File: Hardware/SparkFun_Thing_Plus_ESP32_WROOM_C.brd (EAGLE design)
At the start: 22.9 x 58.4 mm, 108 parts, among them J2 MICRO-SDFRICTION, J3 QWIIC_RA, J5 THING_PLUS, Q2 MBT3904DW1T1, Q3 20V/4.2A/52mΩ/1.4W, U1 MCP73831, U2 ESP-WROOM-3232D-NARROW, U3 XC6222B331MR-G, U4 MAX17048, U5 XC6222B331MR-G, U7 CH340C

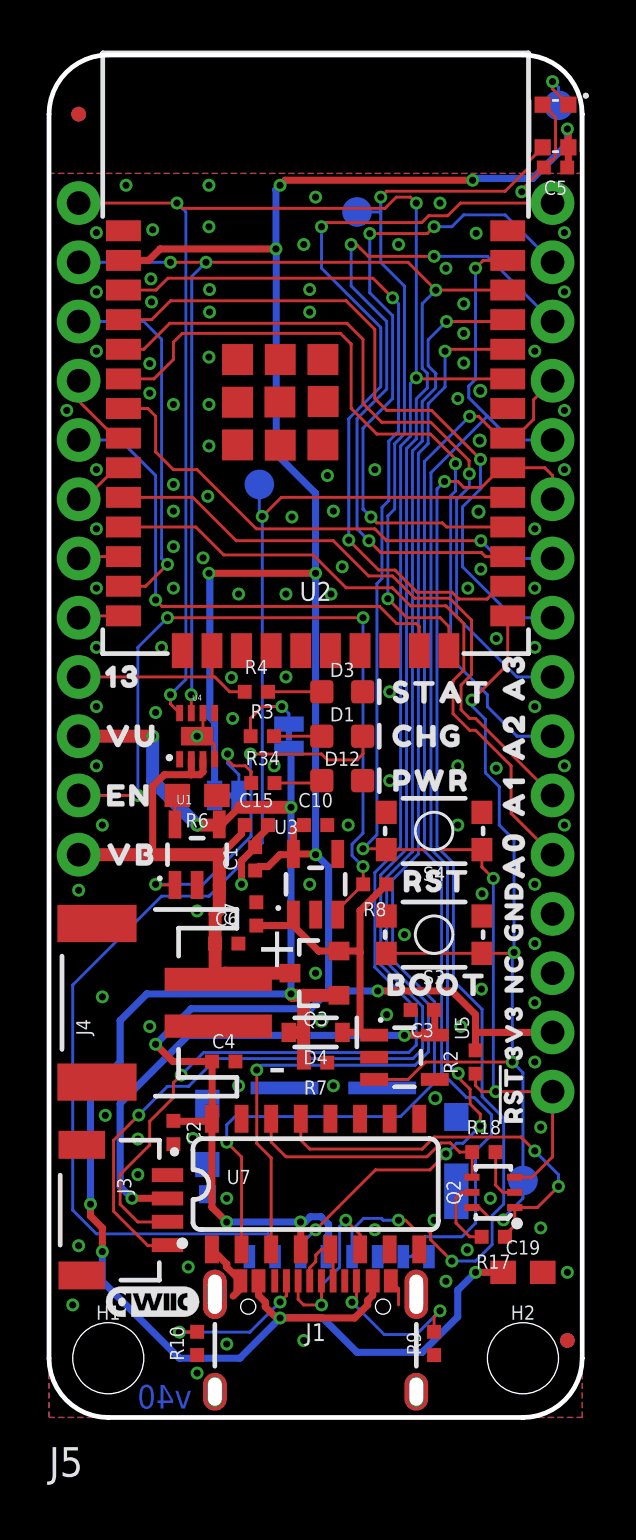
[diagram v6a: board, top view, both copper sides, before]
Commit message: Completed updates post DR.
Schematic:
Change all  text to vector, 8%
Add row lines to boot mode table
Add NC jumper on USB-C shield.
Change 0.1u cap to 10u next to uSD.
Update uSD device to pull in newest changes to keepout.
Label LED jumpers JP1, JP2
Change ADC2 note to say “Is not available when wifi enabled.”
Rearrange schematic to make ESP32 notes fit in box when vectored font.
Change symbol for SOT-25 VREGs to remove NC pin.
Add Nate’s Thing Plus symbol to the SFE libs and make the board change to be logical instead of physical.

Board:
Space out top RGB LED per Dryw’s design
Add dimensions to the uSD card and it’s protrusion.
Add pin 1 indicator for CH340, it’s covered.
Add designed/revised by to board.
Move C19 close to batt charge IC, remove top silk on EN/VB to make it fit if necessary.
Change the width of V_USB to be consistent across the board.
Aim for 30 mil, that’s a 60deg increase at 2A
Got 22 mil all around, best I could do
Change GND, 3.3, NC bottom silk to be pill-style
Fit a flame logo on top.
Acid traps
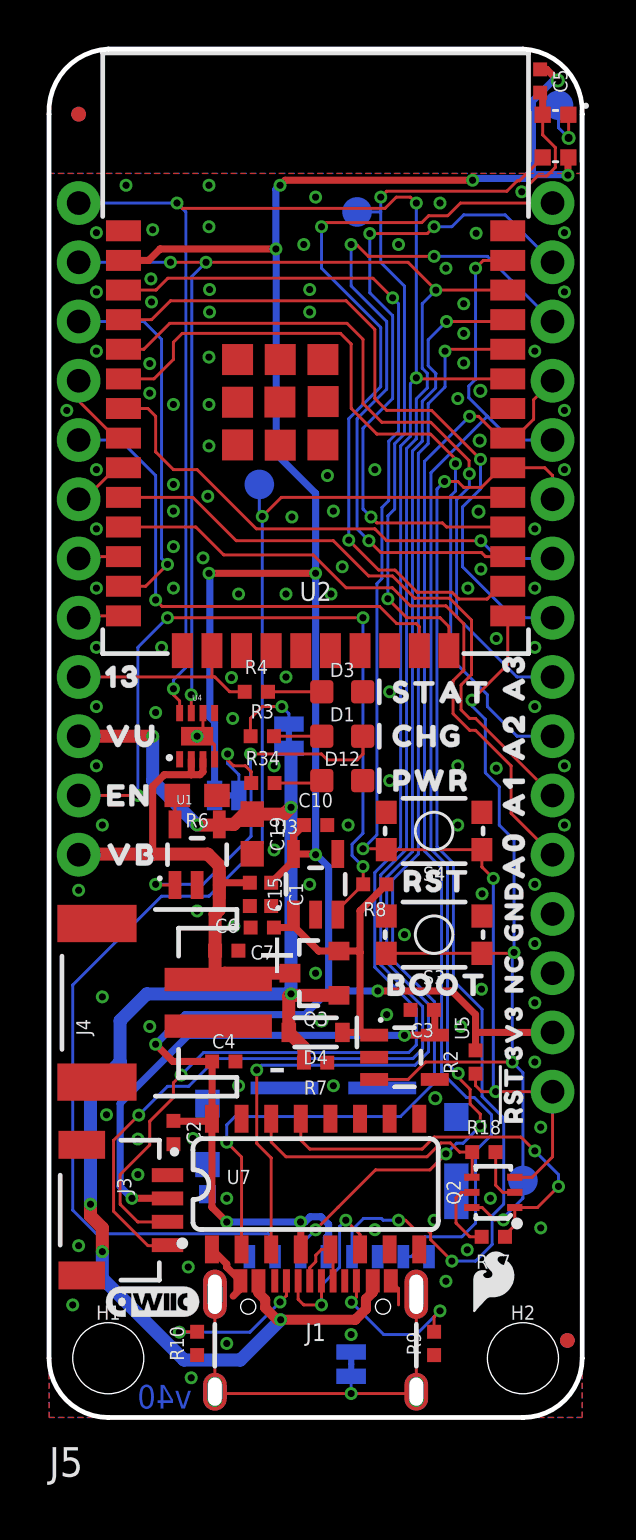
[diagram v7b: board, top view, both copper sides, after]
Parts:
- removed U$106: (no value), output:NC0
- removed U$108: (no value), output:3V30
- removed U$56: (no value), output:GND1
- added JP3: JUMPER-SMT_2_NC_TRACE_SILK, SparkFun-Jumpers:SMT-JUMPER_2_NC_TRACE_SILK
- added U$10: (no value), output:#_NC#0
- added U$11: (no value), output:#_3V3#0
- added U$12: (no value), SparkFun-Aesthetics:SFE_LOGO_FLAME_.1
- added U$8: (no value), output:#SHLD#0
- added U$9: (no value), output:#_GND#0
- C5: value 0.1uF -> 10uF
- J5: value THING_PLUS -> THING_PLUS_LOGICAL
- JP1, JP2: value (none) -> JUMPER-SMT_2_NC_TRACE_SILK
- moved C19 22.1 mm to (8.71, 25.0), turned to 270 degrees
- moved LOGO1 4.38 mm to (7.01, 18.0)
- moved C5 3.77 mm to (21.1, 57.3), turned to 270 degrees
- moved C15 2.98 mm to (8.61, 22.4), turned to 270 degrees
- moved C1 1.67 mm to (9.53, 22.4), turned to 270 degrees
- moved C7 0.64 mm to (9.14, 21.0), turned to 180 degrees
- moved D5 0.43 mm to (21.7, 54.9)
- moved C6 0.30 mm to (7.62, 20.0)
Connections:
- net ESP_12/TP_8 renamed ESP_12/GPIO1
- net ESP_13/TP_9/LED renamed ESP_13/GPIO0/LED
- net ESP_14/TP_3 renamed ESP_14/GPIO6
- net ESP_15/TP_5 renamed ESP_15/GPIO4
- net ESP_27/TP_7 renamed ESP_27/GPIO2
- net ESP_32/TP_4 renamed ESP_32/GPIO5
- net ESP_33/TP_6 renamed ESP_33/GPIO3
- new net N$8: J1.SHLD1, J1.SHLD2, J1.SHLD3, J1.SHLD4, JP3.2
- net GND: now also JP3.1
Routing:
- net N$8: track 0.00 -> 17.8 mm, vias 0 -> 1
- net V_USB: track 77.1 -> 64.9 mm, vias 8 -> 7
- net 3.3V: track 115.9 -> 119.1 mm, vias 11 -> 12
- net GND: track 14.0 -> 11.8 mm
- net VIN: track 13.6 -> 12.9 mm
- net V_BATT: track 23.0 -> 22.3 mm
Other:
- board size 22.9 x 58.4 mm -> 22.9 x 58.7 mm
- board text added: "Alex Brudner"
- board text added: "Nathan Seidle"
- board text added: "Revised by:"

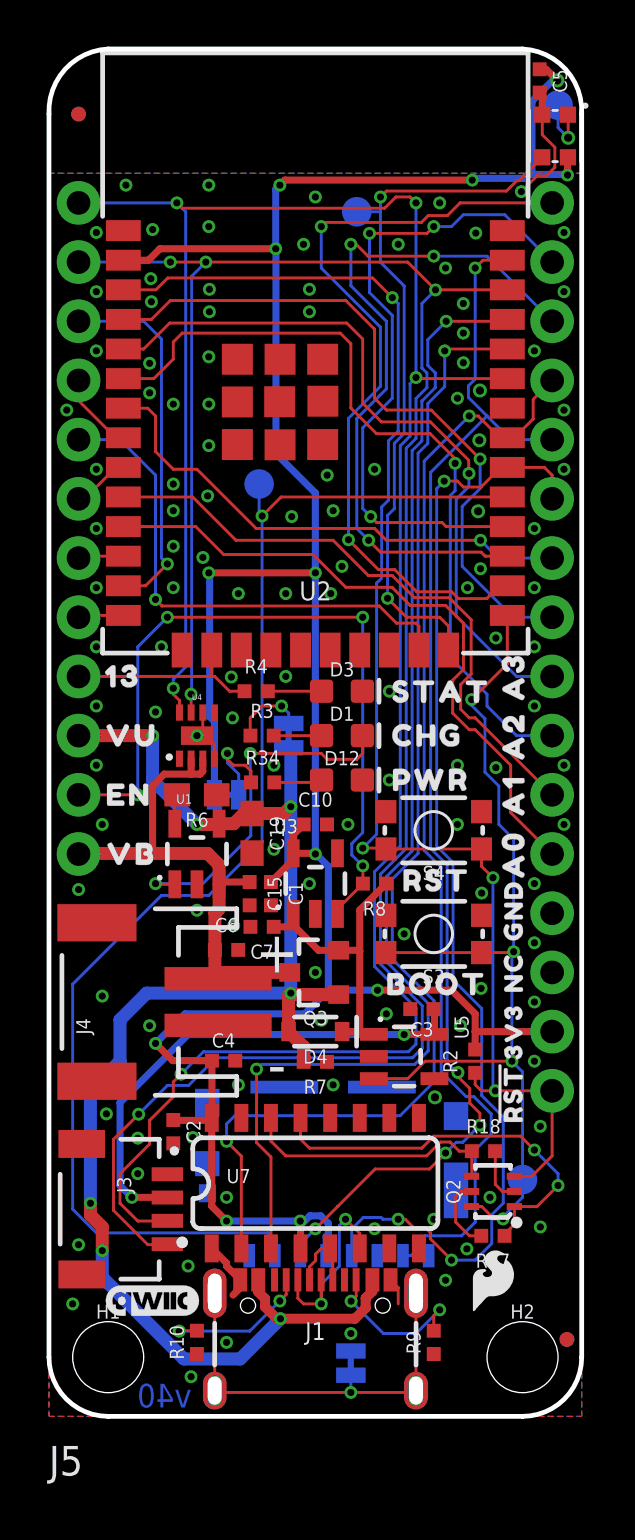
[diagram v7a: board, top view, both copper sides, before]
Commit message: Update post DR changes.
Minor movement edits.
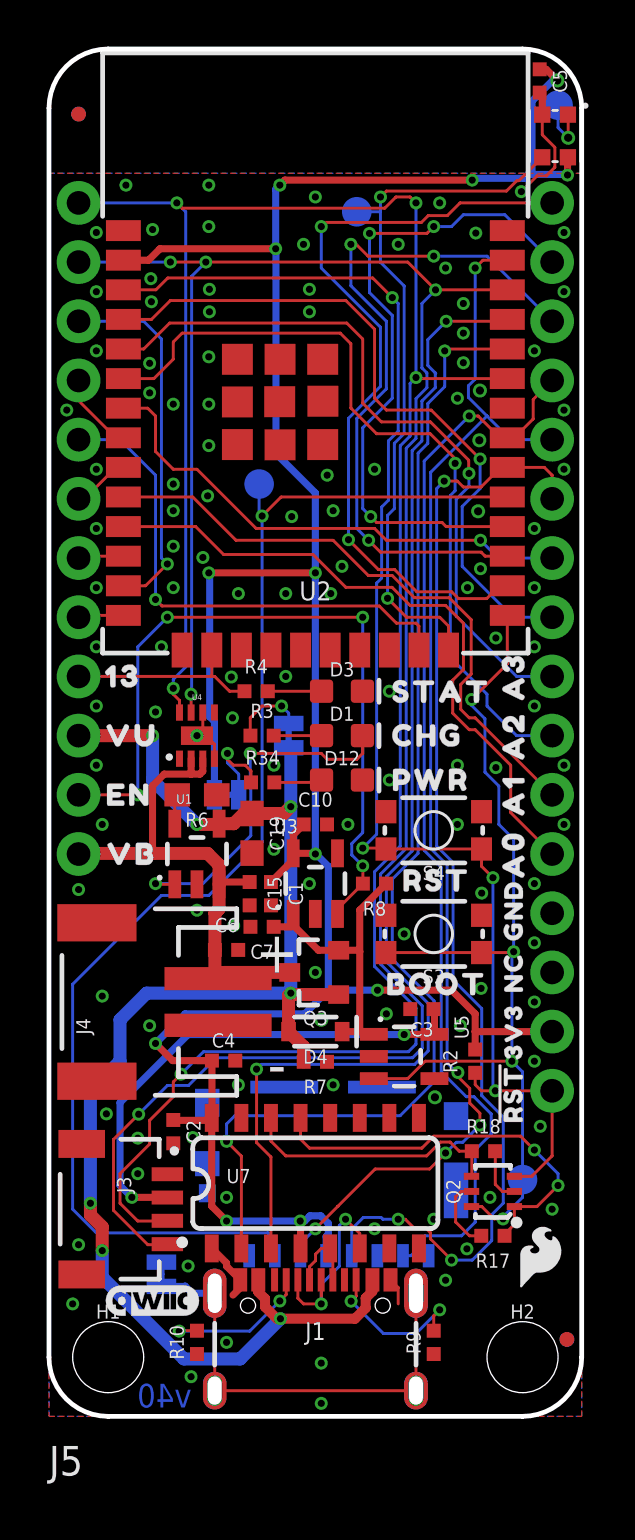
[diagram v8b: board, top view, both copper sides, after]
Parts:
- removed U$59: (no value), SparkFun-Aesthetics:ORDERING_INSTRUCTIONS
- moved LOGO2 19.2 mm to (2.46, 13.0)
- moved U$1 16.8 mm to (21.3, 6.86)
- moved JP3 8.98 mm to (4.83, 6.10)
- moved U$8 8.77 mm to (4.83, 6.93), turned to 90 degrees
- moved U$12 2.27 mm to (21.1, 6.86)
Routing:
- net N$8: track 17.8 -> 19.4 mm, vias 1 -> 0
- net GND: vias 119 -> 120
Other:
- outline, holes or cut-outs redrawn
